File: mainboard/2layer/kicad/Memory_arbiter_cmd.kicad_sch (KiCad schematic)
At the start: 16 parts, among them U19 74LS08, U2 74LS74, U21 74LS51, U38 74LS08, U40 74LS10, U57 74LS04, U60 74LS95, U61 74LS74, Y1 14MHz

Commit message: Fixes for PCB DRC: trace clearance, footprints, board edges
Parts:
- Y1: footprint Crystal:Crystal_HC18-U_Vertical -> Cobra_original:Crystal_HC18-U_Vertical
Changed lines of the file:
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@@
       (effects (font (size 1.27 1.27)))
     )
-    (property "Footprint" "Crystal:Crystal_HC18-U_Vertical" (at 31.75 134.62 0)
+    (property "Footprint" "Cobra_original:Crystal_HC18-U_Vertical" (at 31.75 134.62 0)
       (effects (font (size 1.27 1.27)) hide)
     )

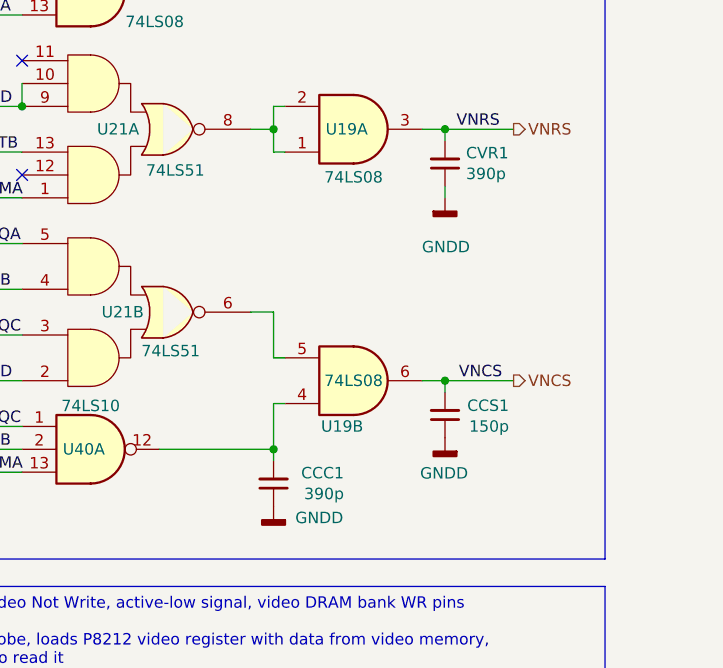
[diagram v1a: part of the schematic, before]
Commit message: More fixes after running DRC. Silskcreen overlaps, other warnings
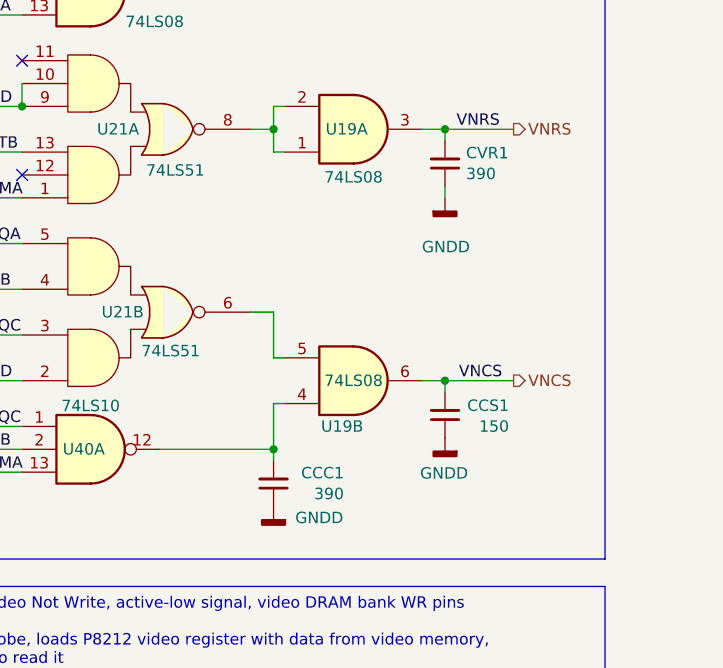
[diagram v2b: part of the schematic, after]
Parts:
- CCC1, CVR1: value 390p -> 390
- CCS1: value 150p -> 150
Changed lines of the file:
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@@
       (effects (font (size 1.27 1.27)) (justify right))
     )
-    (property "Value" "390p" (at 177.5968 91.313 0)
+    (property "Value" "390" (at 177.5968 91.313 0)
       (effects (font (size 1.27 1.27)) (justify right))
     )
@@
       (effects (font (size 1.27 1.27)) (justify right))
     )
-    (property "Value" "390p" (at 164.0332 126.873 0)
+    (property "Value" "390" (at 164.0332 126.873 0)
       (effects (font (size 1.27 1.27)) (justify right))
     )
@@
       (effects (font (size 1.27 1.27)) (justify right))
     )
-    (property "Value" "150p" (at 182.372 119.38 0)
+    (property "Value" "150" (at 182.372 119.38 0)
       (effects (font (size 1.27 1.27)) (justify right))
     )
